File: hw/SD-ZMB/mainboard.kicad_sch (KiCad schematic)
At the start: 52 parts, among them J1 HDR 1x02 Pin, SW1 SW_Push, U1 12MHz, U10 74F260, U11 74AHCT74DR, U12 74ACT138D, U13 Z80CPU, U14 74F27, U15 SRAM 8K/32K, U16 74ACT138D, U17 74AHC541NS, U18 74AHCT245NS, U19 74AHCT10, U2 74AHCT74DR, U20 74AC11, U21 AS6C4008, U22 SST39SF040, U23 74AHCT244NS, U24 74AHCT244NS, U25 74AHCT245NS, U26 74AHCT245NS, U27 74AHCT245NS, U28 74HCT273NS, U29 74F27, U3 MIC2775, U30 74AHCT245NS, U34 74AHCT10, U38 74AHCT32, U4 74AHCT08, U5 74AHCT08, U6 74AHCT00, U7 74AHCT02, U8 74AHCT00, U9 74AHCT32

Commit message: ZMB: v1.0 Board RFP
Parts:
- removed U24: 74AHCT244NS, Package_SO:SOIC-20W_7.5x12.8mm_P1.27mm, symbol AES_Library:74244_OI-AES
- added C36, C37: 330.0pF, Capacitor_SMD:C_0603_1608Metric, symbol Device:C_Small
- added D5, D7: BAS7002VH6327XTSA1, Diode_SMD:D_SOD-523, symbol Device:D_Schottky_Small_Filled
- added OP1: AES-Opt_1_of_2, Connector_PinHeader_2.00mm:PinHeader_1x03_P2.00mm_Vertical, symbol AES_Library:AES-Opt_1_of_2
- added OP4: CONN 2x3 HDR, AES_Library:PinHeader_2x03_AB_2mm-AES, symbol Connector_Generic:Conn_02x03_Row_Letter_First
- added R14, R5: 27.4, Resistor_SMD:R_0805_2012Metric, symbol Device:R_Small_US
- added R19, R21: 22, Resistor_SMD:R_0805_2012Metric, symbol Device:R_Small_US
- added R26, R34, R35, R36: 10k, Resistor_SMD:R_0805_2012Metric, symbol Device:R_Small_US
- added unit 2 of U2
- added unit 2 of U20
- added U24: 74AHCT244NS, Package_SO:SO-20_5.3x12.6mm_P1.27mm, symbol AES_Library:74244-AES
- added U32: 74AHCT74, Package_SO:SOIC-14_3.9x8.7mm_P1.27mm, symbol 74xx:74HC74
- added unit 4 of U38
- added unit 3 of U38
- added U39: 74AHCT04, Package_SO:SOIC-14_3.9x8.7mm_P1.27mm, symbol AES_Library:7404-AES
- added U40: 74LVC1G06W, Package_TO_SOT_SMD:SOT-23-5, symbol AES_Library:74LVC1G06-AES
- added U41: 74LV21, Package_SO:SOIC-14_3.9x8.7mm_P1.27mm, symbol 74xx:74LS21
- added U42: 74F260, Package_SO:SOIC-14_3.9x8.7mm_P1.27mm, symbol AES_Library:74F260-AES
- added U44: 74LVC125AS, Package_SO:SOIC-14_3.9x8.7mm_P1.27mm, symbol 74xx:74LVC125
- C1: footprint Capacitor_SMD:C_0603_1608Metric_Pad1.08x0.95mm_HandSolder -> Capacitor_SMD:C_0603_1608Metric
- D1, D2, D3, D4: footprint LED_SMD:LED_0805_2012Metric_Pad1.15x1.40mm_HandSolder -> LED_THT:LED_D3.0mm
- OP5: renamed from OPT1; footprint AES_Library:PinHeader_2x03_AB-AES -> AES_Library:PinHeader_2x03_AB_2mm-AES; Opt-2 50/50 -> ROM/RAM; When PAGING OFF -> NOPG RAM/ROM
- R1, R2, R3, R4: footprint Resistor_SMD:R_0805_2012Metric_Pad1.20x1.40mm_HandSolder -> Resistor_SMD:R_0805_2012Metric
- U1: value 12MHz -> 12MHz Can Osc; footprint Package_DIP:DIP-14_W7.62mm_LongPads -> AES_Library:OSC-8_14-AES
- U11, U2: value 74AHCT74DR -> 74AHCT74
- U11: renamed from U2; value 74AHCT74DR -> 74AHCT74
- U17: value 74AHC541NS -> 74AHC541; footprint Package_SO:SOIC-20W_7.5x12.8mm_P1.27mm -> Package_SO:SO-20_5.3x12.6mm_P1.27mm
- U18: value 74AHCT245NS -> 74AHCT245; footprint Package_SO:SOIC-20W_7.5x12.8mm_P1.27mm -> Package_SO:SO-20_5.3x12.6mm_P1.27mm; symbol AES_Library:74HC245_BA-AES -> AES_Library:74245_BA-AES
- U19, U34: value 74AHCT10 -> 74ACT10
- U20: value 74AC11 -> 74ACT11; PropDly (10nS) -> (9nS)
- U23: footprint Package_SO:SOIC-20W_7.5x12.8mm_P1.27mm -> Package_SO:SO-20_5.3x12.6mm_P1.27mm; PropDly (12nS) -> (12ns)
- U25, U26, U27, U30: value 74AHCT245NS -> 74AHCT245; footprint Package_SO:SOIC-20W_7.5x12.8mm_P1.27mm -> Package_SO:SO-20_5.3x12.6mm_P1.27mm
- U28: footprint Package_SO:SOIC-20W_7.5x12.8mm_P1.27mm -> Package_SO:SO-20_5.3x12.6mm_P1.27mm
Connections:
- net BD_OPT1- is gone; now on net BRD-: RN6.7 (R6)
- net +5V: now also R26.1, R34.2, R35.2, R36.2, U24.20 (VCC), U40.5 (VCC)
- net BA12: now also RN3.9 (R8), U24.12 (O3a), U24.9 (O0b); no longer RN3.6 (R5)
- net BA13: now also RN3.6 (R5), U24.18 (O0a), U24.3 (O3b); no longer RN3.7 (R6)
- net BA14: now also RN3.7 (R6), U24.16 (O1a), U24.5 (O2b); no longer RN3.8 (R7)
- net BA15: now also RN3.8 (R7), U24.14 (O2a), U24.7 (O1b); no longer RN3.9 (R8)
- net BIORQ-: now also RN6.9 (R8); no longer RN6.5 (R4)
- net BMREQ-: now also RN6.5 (R4); no longer RN6.4 (R3)
- net BRD-: no longer RN6.2 (R1)
- net BRDRST: now also U40.2
- net BRDRST-: now also R26.2, U20.3, U20.4, U32.13 (~{R}), U40.4; no longer U3.1 (~{RST})
- net BWR-: now also RN6.6 (R5); no longer RN6.3 (R2)
- net GND: now also C36.2, C37.2, U2.12 (D), U24.10 (GND), U32.12 (D), U32.2 (D), U40.3 (GND)
- net MHA13: now also U24.2 (I0a)
- net MHA14: now also U24.4 (I1a)
- net MHA15: now also U24.6 (I2a)
- net MHAtoBA-: now also U24.1 (~{OEa})
- net NMIEN: now also U39.11; no longer U8.1, U8.2
- net VPU1: now also OP5.a1 (Pin_a1), R35.1; no longer RN6.8 (R7)
- net VPU2: now also OP1.1 (Pin_A), R34.1; no longer OP5.a1 (Pin_a1), RN6.9 (R8), U11.1 (~{R}), U11.10 (~{S}), U15.26 (A13/CE_{2})
- net ZA12: now also U24.11 (I0b), U24.8 (I3a)
- net ZA13: now also U24.13 (I1b)
- net ZA14: now also U24.15 (I2b)
- net ZA15: now also U24.17 (I3b)
- net ZAtHoBA-: now also U24.19 (~{OEb})
- net ZBREQ-: now also RN6.8 (R7); no longer RN6.6 (R5)
- net ZCLK: now also OP4.b1 (Pin_b1), OP4.b2 (Pin_b2), OP4.b3 (Pin_b3)
- net ZINT-: now also U42.3
- net ZIORQ-: now also U41.5, U42.10, U42.11, U42.9
- net ZM1-: now also U42.12
- net ZMREQ-: now also U39.5
- net at U8.3: now also U2.10 (~{S}); no longer U9.2
- net CLK renamed CLKf
- net CLKf: now also OP4.a2 (Pin_a2), U39.9, U41.2, U42.2, U42.8, U44.5; no longer U2.5 (Q)
- net CLK2RST- renamed CLKhRST-
- net CLKhRST-: now also OP1.2 (Pin_Common)
- net CPURST- renamed CRSTRQ-
- net FSCLK- renamed FRCCLKf
- net FRCCLKf: now also U39.3
- net USR5 renamed RCBPAGE
- net USR6 renamed DSPBLON-
- new net: U20.6, U32.4 (~{S})
- new net: C36.1, D5.2 (A), R5.2, U44.1
- new net: U20.5, U38.8
- new net: U38.12, U42.6
- new net: C37.1, D7.2 (A), R14.2, U44.4
- new net: R21.1, U44.6
- new net: U39.10, U9.2
- new net: U38.13, U42.5
- new net: R19.1, U44.3
- new net: OP4.a1 (Pin_a1), R19.2, R21.2
- new net CLKf-: U2.11 (C), U39.8
- new net CLKfEN-: D7.1 (K), R14.1, U32.8 (~{Q}), U38.9
- new net CLKfFRC-: U2.13 (~{R}), U32.1 (~{R}), U39.1, U39.4
- new net CLKfSET-: U32.10 (~{S}), U32.5 (Q)
- new net CLKfSW: U32.3 (C), U41.6
- new net CLKh: OP4.a3 (Pin_a3), U2.5 (Q), U41.1, U44.2
- new net CLKhEN-: D5.1 (K), R5.1, U32.9 (Q), U8.1
- new net CLKhRR-: OP1.3 (Pin_B), U2.8 (~{Q})
- new net CLKhSW: U32.11 (C), U38.11, U8.2
- new net CTRLCLK-: U38.10, U39.2, U42.1, U42.4
- new net VPU1N: RN6.2 (R1), U15.26 (A13/CE_{2})
- new net VPU2N: RN6.3 (R2)
- new net VPU3: R36.1, U11.1 (~{R}), U11.10 (~{S})
- new net VPU3N: RN6.4 (R3)
- new net ZMREQ: U39.6, U42.13
- new net bpIEO: U41.4
- no-connect marks 9 -> 11
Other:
- moved on the sheet: D1, D2, D3, D4, R1, R2, R3, R4, U10A, U14A, U14C, U19A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

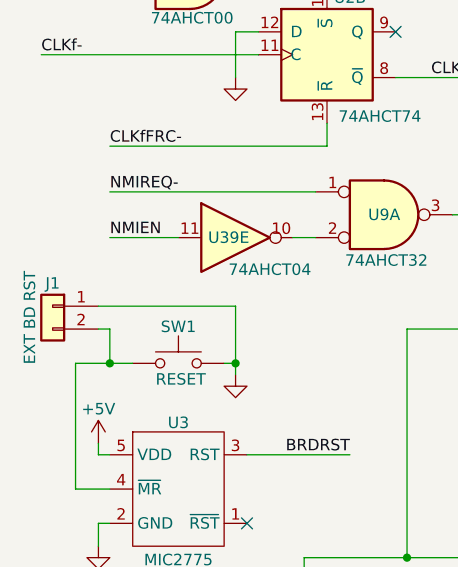
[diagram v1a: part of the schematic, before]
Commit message: ZMB gerbers created. OLED display portion updates.
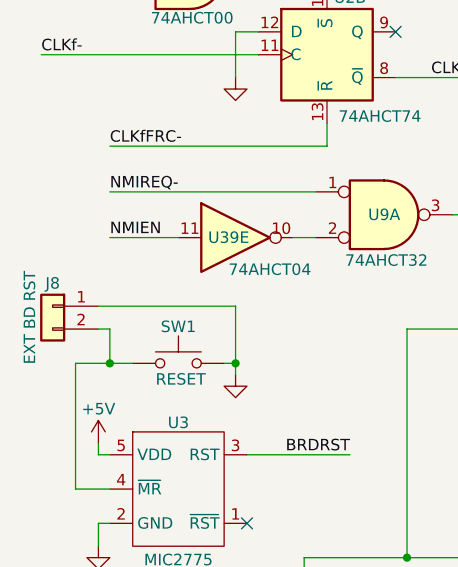
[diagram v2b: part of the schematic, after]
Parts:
- renumbered J1 to J8
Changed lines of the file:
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@@
 		(on_board yes)
 		(dnp no)
-		(property "Reference" "J1"
+		(property "Reference" "J8"
 			(at 16.51 107.95 0)
 			(effects
@@
 			(project ""
 				(path "/62236e9f-ef27-467c-852b-587c32c473f1/48cc9b60-debe-432c-ac2c-bb1cba6b9068"
-					(reference "J1")
+					(reference "J8")
 					(unit 1)
 				)

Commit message: PCB received
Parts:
- renumbered U13 to U10, U21 to U11, U22 to U12, U7 to U13, U29 to U14, U5 to U15, U9 to U16, U4 to U17, U25 to U18, U3 to U2, U14 to U20, U26 to U21, U16 to U23, U23 to U25, U6 to U27, U8 to U28, U11 to U29, U27 to U3, U12 to U30, U17 to U31, U18 to U32, U1 to U34, U32 to U35, U2 to U38, U38 to U39, U10 to U4, U42 to U40, U39 to U41, U28 to U42, U41 to U45, U20 to U46, U15 to U5, U30 to U6, U34 to U7, U40 to U9

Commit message: ECO.A: PG Reg A3 incorrect. Change U17B AND to SPR.1A OR
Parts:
- removed unit 2 of U17
- added SPR.1: 74AHCT32, symbol 74xx:74LS32
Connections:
- net PRA3: now also SPR.1.3
- net ZA0: now also SPR.1.1
- net ZIORQ-: now also SPR.1.2
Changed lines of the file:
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@@
 	(title_block
 		(title "Z80, Clk, Rst, Decode, Mem")
-		(date "2025-10-19")
-		(rev "PR8.2")
+		(date "2026-02-07")
+		(rev "PR8.2.A")
 		(company "SilkyDESIGN")
 		(comment 1 "Copyright 2025 AESilky & SMcCown")
@@
 	)
 	(symbol
+		(lib_id "74xx:74LS32")
+		(at 119.38 148.59 0)
+		(unit 1)
+		(convert 2)
+		(exclude_from_sim no)
+		(in_bom yes)
+		(on_board yes)
+		(dnp no)
+		(property "Reference" "SPR.1"
+			(at 119.38 148.844 0)
+			(effects
+				(font
+					(size 1.27 1.27)
+				)
+			)
+		)
+		(property "Value" "74AHCT32"
+			(at 119.38 153.67 0)
+			(effects
+				(font
+					(size 1.27 1.27)
+				)
+			)
+		)
+		(property "Footprint" ""
+			(at 119.38 148.59 0)
+			(effects
+				(font
+					(size 1.27 1.27)
+				)
+				(hide yes)
+			)
+		)
+		(property "Datasheet" "http://www.ti.com/lit/gpn/sn74LS32"
+			(at 119.38 148.59 0)
+			(effects
+				(font
+					(size 1.27 1.27)
+				)
+				(hide yes)
+			)
+		)
+		(property "Description" "Quad 2-input OR"
+			(at 119.38 148.59 0)
+			(effects
+				(font
+					(size 1.27 1.27)
+				)
+				(hide yes)
+			)
+		)
+		(pin "6"
+		)
+		(pin "11"
+		)
+		(pin "2"
+		)
+		(pin "5"
+		)
+		(pin "13"
+		)
+		(pin "1"
+		)
+		(pin "12"
+		)
+		(pin "4"
+		)
+		(pin "3"
+		)
+		(pin "9"
+		)
+		(pin "10"
+		)
+		(pin "8"
+		)
+		(pin "14"
+		)
+		(pin "7"
+		)
+		(instances
+			(project "SD-ZMB"
+				(path "/62236e9f-ef27-467c-852b-587c32c473f1/48cc9b60-debe-432c-ac2c-bb1cba6b9068"
+					(reference "SPR.1")
+					(unit 1)
+				)
+			)
+		)
+	)
+	(symbol
 		(lib_id "AES_Library:74245-AES")
 		(at 273.05 140.97 0)
@@
 				)
 			)
-		)
-	)
-	(symbol
-		(lib_id "74xx:74LS08")
-		(at 119.38 148.59 0)
-		(unit 2)
-		(convert 2)
-		(exclude_from_sim no)
-		(in_bom yes)
-		(on_board yes)
-		(dnp no)
-		(property "Reference" "U17"
-			(at 119.634 148.59 0)
-			(effects
-				(font
-					(size 1.27 1.27)
-				)
-			)
-		)
-		(property "Value" "74AHCT08"
-			(at 118.364 153.416 0)
-			(effects
-				(font
-					(size 1.27 1.27)
-				)
-			)
-		)
-		(property "Footprint" "Package_SO:SOIC-14_3.9x8.7mm_P1.27mm"
-			(at 119.38 148.59 0)
-			(effects
-				(font
-					(size 1.27 1.27)
-				)
-				(hide yes)
-			)
-		)
-		(property "Datasheet" "http://www.ti.com/lit/gpn/sn74LS08"
-			(at 119.38 148.59 0)
-			(effects
-				(font
-					(size 1.27 1.27)
-				)
-				(hide yes)
-			)
-		)
-		(property "Description" "Quad And2"
-			(at 119.38 148.59 0)
-			(effects
-				(font
-					(size 1.27 1.27)
-				)
-				(hide yes)
-			)
-		)
-		(property "PropDly" "(9nS)"
-			(at 118.618 150.622 0)
-			(effects
-				(font
-					(size 1.27 1.27)
-				)
-			)
-		)
-		(property "CPU" ""
-			(at 119.38 148.59 0)
-			(effects
-				(font
-					(size 1.27 1.27)
-				)
-				(hide yes)
-			)
-		)
-		(property "OPT-A" ""
-			(at 119.38 148.59 0)
-			(effects
-				(font
-					(size 1.27 1.27)
-				)
-				(hide yes)
-			)
-		)
-		(property "OPT-B" ""
-			(at 119.38 148.59 0)
-			(effects
-				(font
-					(size 1.27 1.27)
-				)
-				(hide yes)
-			)
-		)
-		(pin "5"
-		)
-		(pin "9"
-		)
-		(pin "4"
-		)
-		(pin "14"
-		)
-		(pin "11"
-		)
-		(pin "12"
-		)
-		(pin "7"
-		)
-		(pin "2"
-		)
-		(pin "1"
-		)
-		(pin "6"
-		)
-		(pin "3"
-		)
-		(pin "10"
-		)
-		(pin "8"
-		)
-		(pin "13"
-		)
-		(instances
-			(project "SD-ZMB"
-				(path "/62236e9f-ef27-467c-852b-587c32c473f1/48cc9b60-debe-432c-ac2c-bb1cba6b9068"
-					(reference "U17")
-					(unit 2)
-				)
-			)
